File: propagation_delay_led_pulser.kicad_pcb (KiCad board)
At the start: 2 copper layers, 33 x 48 mm, 16 parts, among them J1 Power/Bias In, J4 Pulse Out, U1 ICM7555xB, U2 74AC14, U3 74AHC1G00

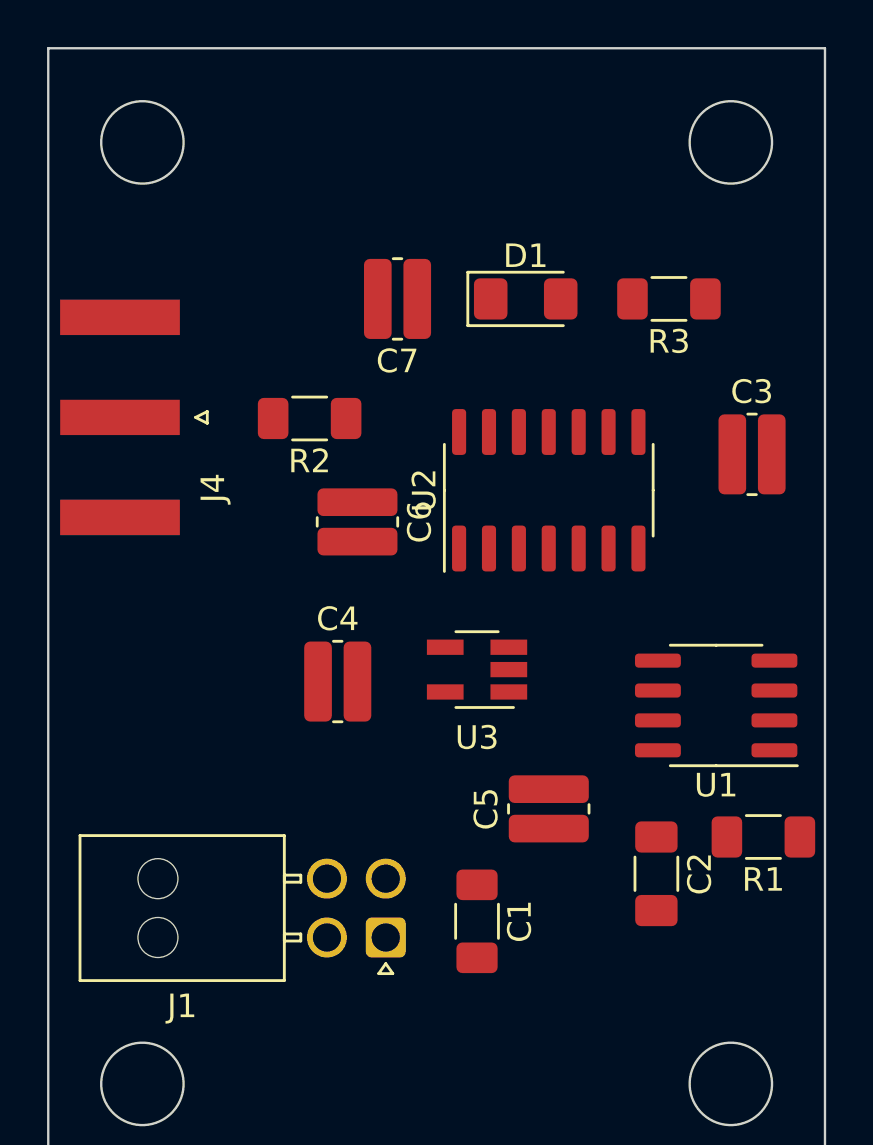
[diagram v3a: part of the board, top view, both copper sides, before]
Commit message: most routing done, need to poar ground plane
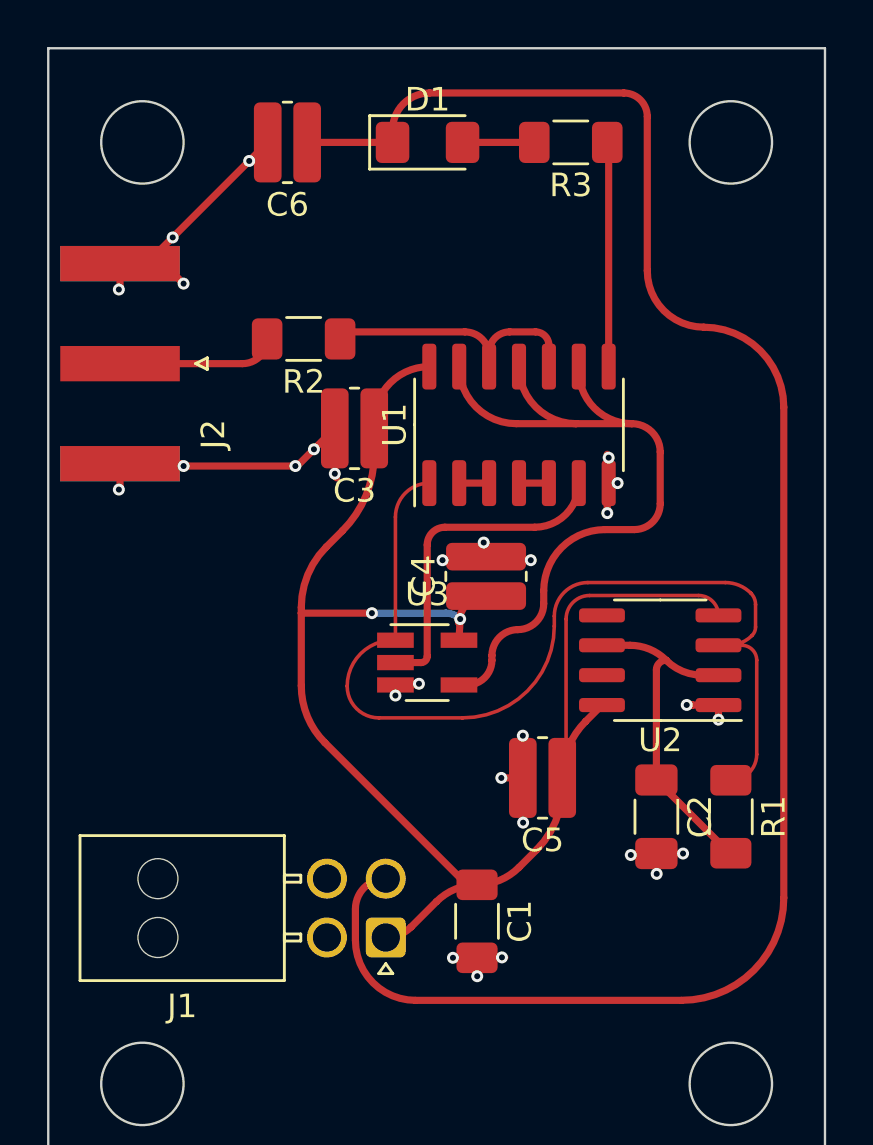
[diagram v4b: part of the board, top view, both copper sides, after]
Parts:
- removed C7: 1u, Resistor_SMD:R_0612_1632Metric_Pad1.18x3.40mm_HandSolder
- removed J4: Pulse Out, Connector_Coaxial:SMA_Amphenol_132289_EdgeMount
- added J2: Pulse Out, Connector_Coaxial:SMA_Amphenol_132289_EdgeMount, F.Cu at (199.5, 61.1)
- C6: value 0.1u -> 1u
- U1: value ICM7555xB -> 74AC14; footprint Package_SO:SOIC-8_3.9x4.9mm_P1.27mm -> Package_SO:SOIC-14_3.9x8.7mm_P1.27mm
- U2: value 74AC14 -> ICM7555xB; footprint Package_SO:SOIC-14_3.9x8.7mm_P1.27mm -> Package_SO:SOIC-8_3.9x4.9mm_P1.27mm
- moved C3 16.9 mm to (209.4, 63.9), turned to 180 degrees
- moved C6 16.4 mm to (206.6, 51.7), turned to 180 degrees
- moved U1 14.6 mm to (216.4, 63.7), turned to 90 degrees
- moved U2 8.64 mm to (222.4, 73.7), turned to 180 degrees
- moved D1 7.85 mm to (212.5, 51.7)
- moved R3 7.85 mm to (218.6, 51.7)
- moved C4 7.72 mm to (215.0, 70.1), turned to 90 degrees
- moved R2 3.39 mm to (207.3, 60.1)
- moved C2 2.42 mm to (222.2, 80.4)
- moved U3 2.14 mm to (212.5, 73.8), turned to 0 degrees
- moved R1 1.63 mm to (225.4, 80.4), turned to -90 degrees
- moved C5 1.34 mm to (217.4, 78.7), turned to 180 degrees
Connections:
- C6 pad 1: VCC -> /LED_Anode
- U1 pad 1: GND -> /Timer_out
- U1 pad 2: /Timer_THR -> /Inv1to2
- U1 pad 3: /Timer_out -> /Inv1to2
- U1 pad 4: VCC -> /Inv2to3
- U1 pad 5: unconnected-(U1-Pad5) -> /Inv2to3
- U1 pad 6: /Timer_THR -> /Inv3toNand
- U1 pad 7: unconnected-(U1-Pad7) -> GND
- U1 pad 8: VCC -> /drive_led_r
- U2 pad 1: /Timer_out -> GND
- U2 pad 2: /Inv1to2 -> /Timer_THR
- U2 pad 3: /Inv1to2 -> /Timer_out
- U2 pad 4: /Inv2to3 -> VCC
- U2 pad 5: /Inv2to3 -> unconnected-(U2-Pad5)
- U2 pad 6: /Inv3toNand -> /Timer_THR
- U2 pad 7: GND -> unconnected-(U2-Pad7)
- U2 pad 8: /drive_led_r -> VCC
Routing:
- net /LED_Anode: track 0.00 -> 77.3 mm
- net VCC: track 0.00 -> 66.2 mm, vias 0 -> 2
- net GND: track 0.00 -> 48.8 mm, vias 0 -> 28
- net /Timer_out: track 0.00 -> 42.9 mm
- net /Pulser_out: track 0.00 -> 33.4 mm
- net /Timer_THR: track 0.00 -> 15.0 mm
- net /Inv3toNand: track 0.00 -> 14.1 mm
- net /drive_pulse_out_r: track 0.00 -> 11.0 mm
- net /drive_led_r: track 0.00 -> 9.54 mm
- net Net-(J2-Pad1): track 0.00 -> 6.81 mm
- net Net-(D1-Pad2): track 0.00 -> 3.05 mm
- net /Inv2to3: track 0.00 -> 1.27 mm
- net /Inv1to2: track 0.00 -> 1.27 mm

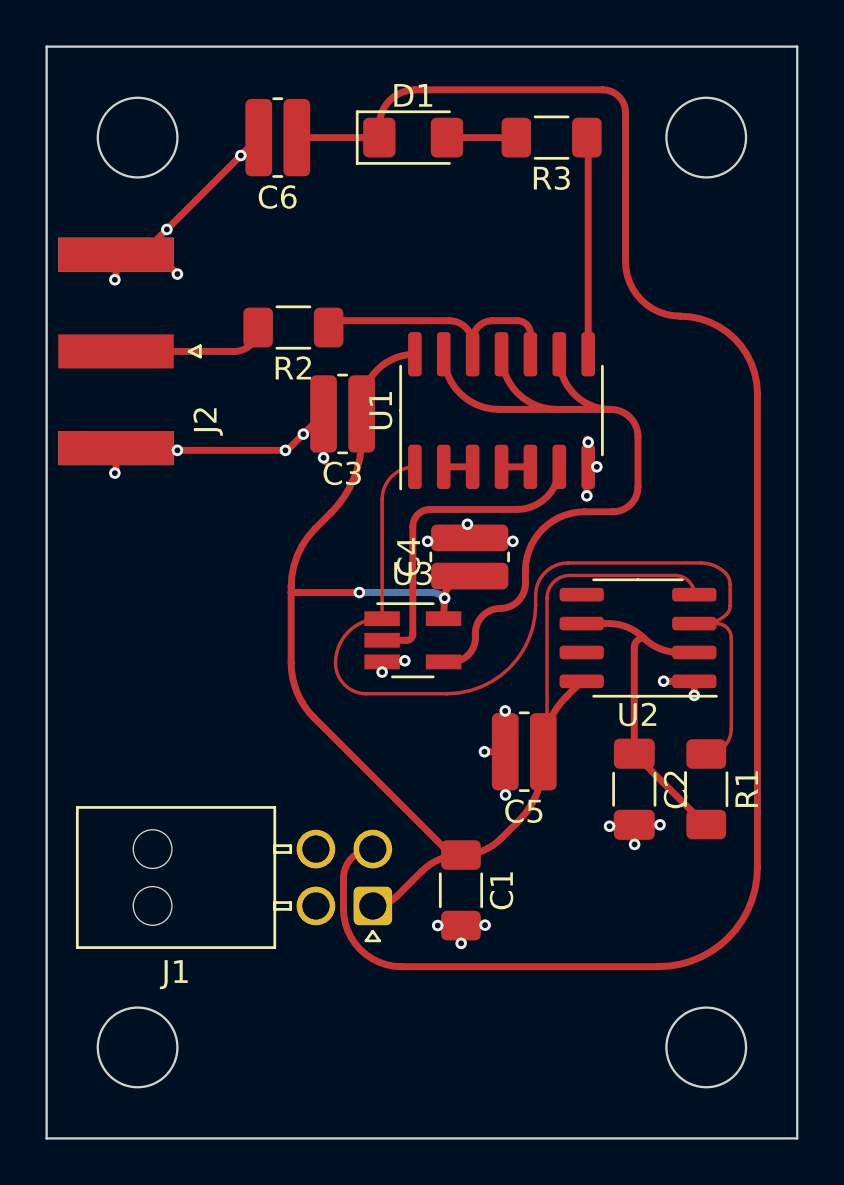
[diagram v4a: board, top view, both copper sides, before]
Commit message: PCB layout complete
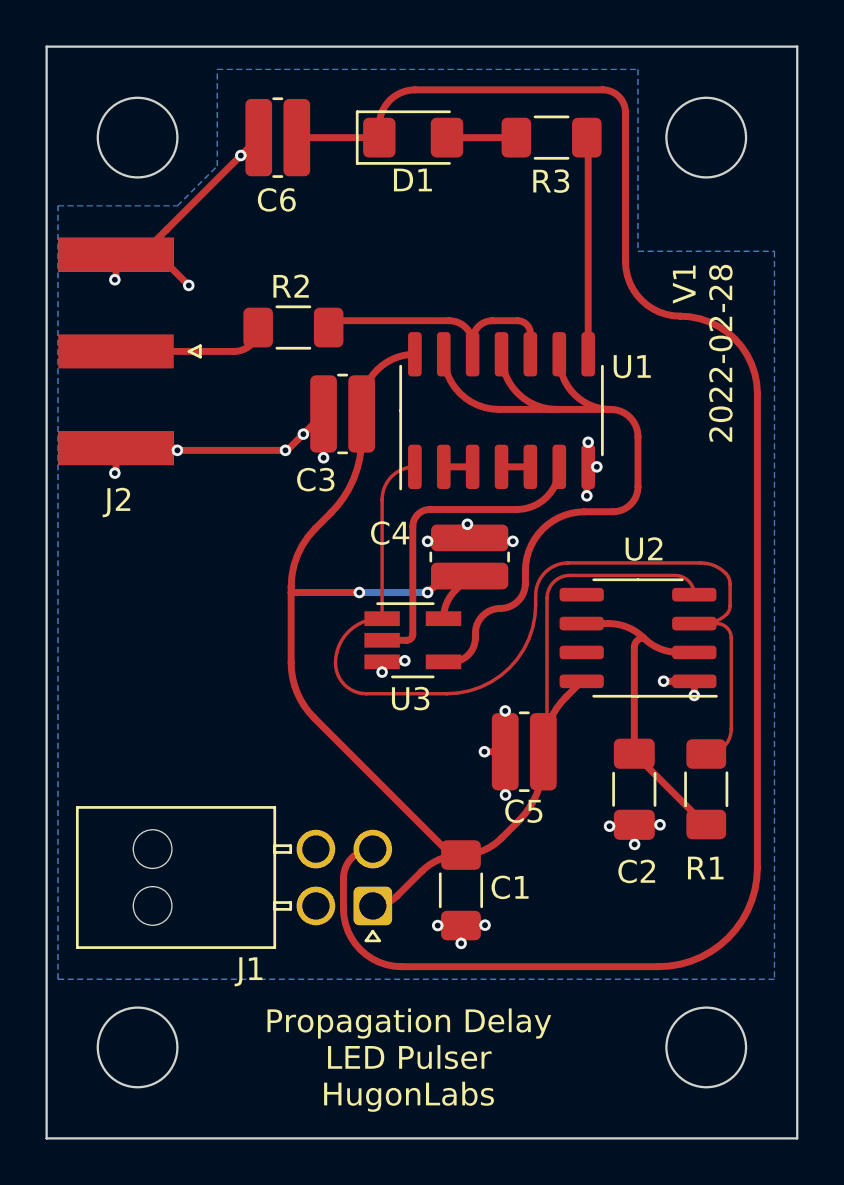
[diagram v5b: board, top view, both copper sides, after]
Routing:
- net /Pulser_out: track 33.4 -> 32.8 mm
- net GND: track 48.8 -> 48.3 mm, vias 28 -> 27
- added copper zone on B.Cu, net GND
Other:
- board text added: "Propagation Delay LED Pulser HugonLabs"
- board text added: "Propagation Delay LED Pulser HugonLabs 2022-02-28 V1"
- board text added: "V1 2022-02-28"
